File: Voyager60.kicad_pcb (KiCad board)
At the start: 2 copper layers, 285 x 95.1 mm, 265 parts, among them Q1 2N7002, SW1 5.2x5.2mm, U1 ATmega32U4-MU, U2 PRTR5V0U2X, Y1 16Mhz

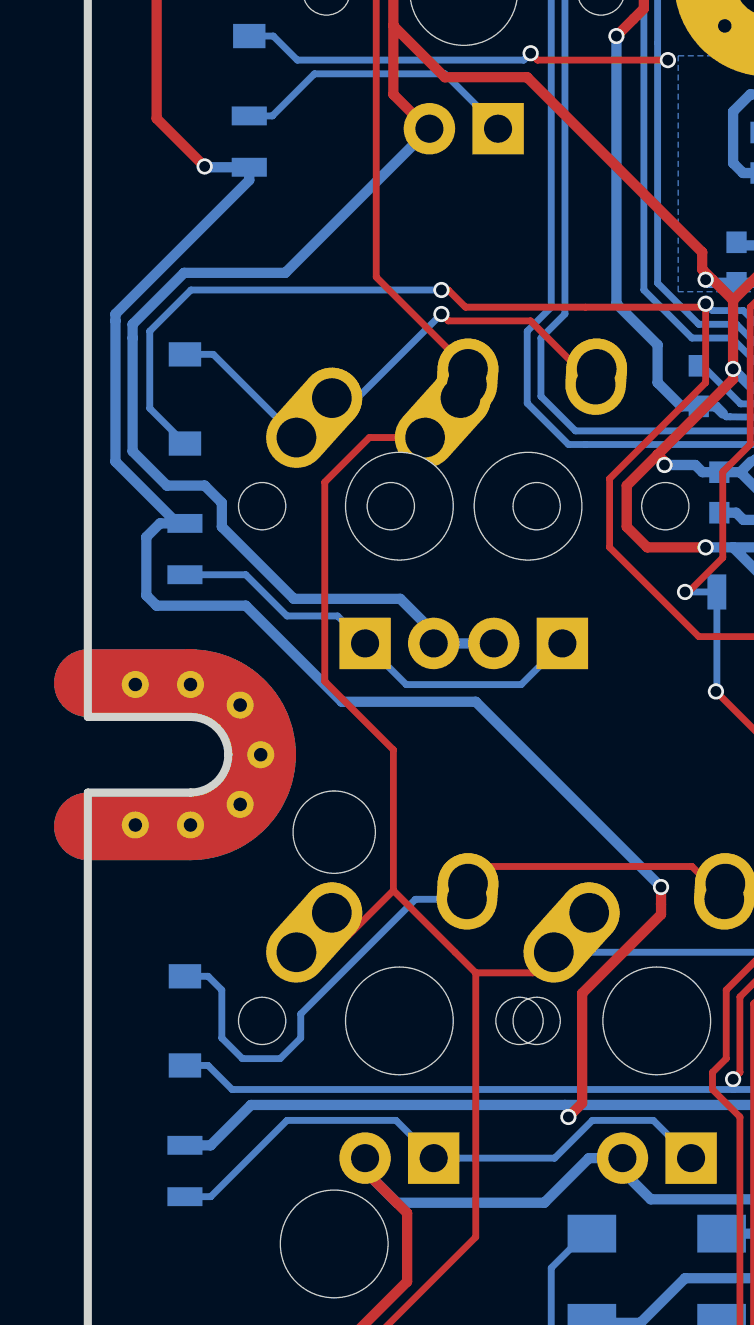
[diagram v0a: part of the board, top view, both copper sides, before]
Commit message: Alps Stepped Caps Lock
Added alps stepped caps lock support at the cost of removing caps lock LED support.
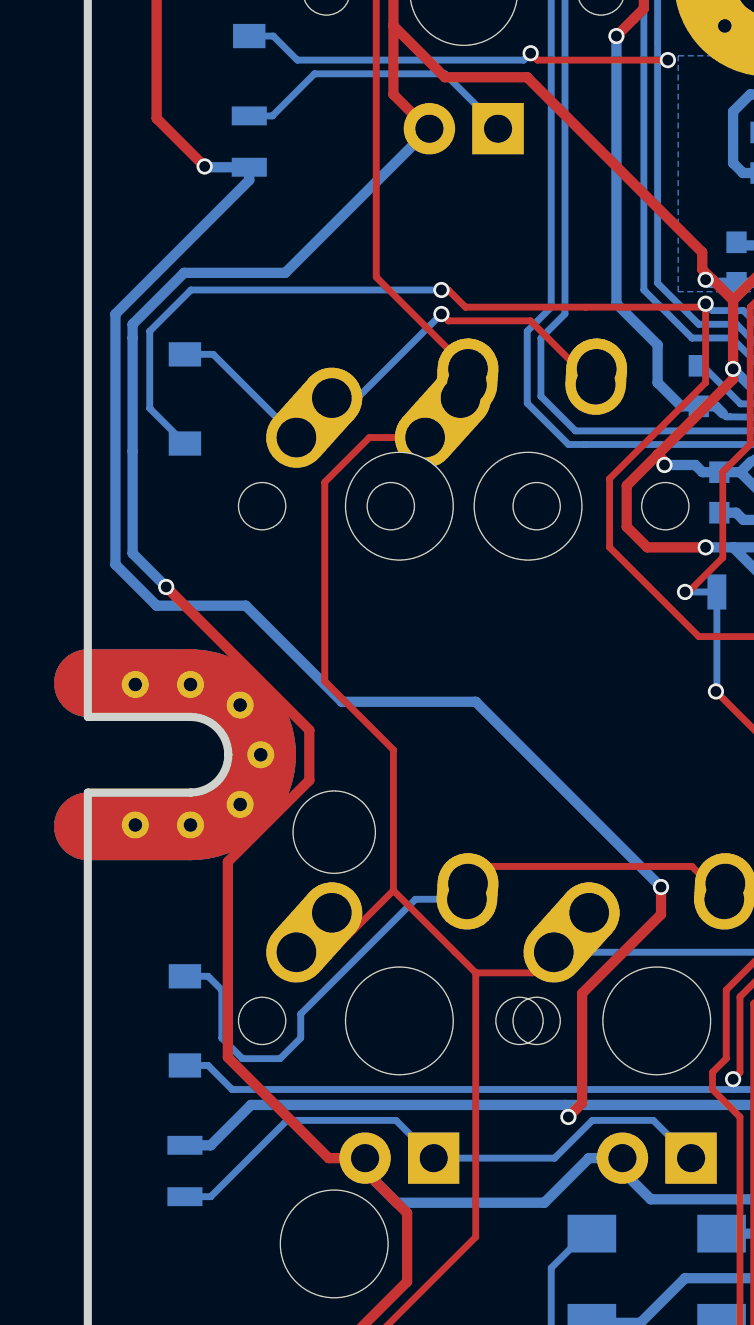
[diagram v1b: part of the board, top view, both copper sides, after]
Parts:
- removed R31: 1k, Resistors_SMD:R_0805
- K_CAPS1: value MX-1.75U -> 1.75U; footprint MX_Alps_Hybrid:MX-1.75U -> MX_Alps_Hybrid:MX-1.75U-NoLED
- K_CAPS2: footprint MX_Alps_Hybrid:MX-1.25U-FLIPPED -> MX_Alps_Hybrid:MX-1.25U-NoLED
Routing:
- net Net-(K_CAPS1-Pad4): track 16.3 -> 0.00 mm
- net +5V: track 1795.4 -> 1811.3 mm, vias 13 -> 14
- net LEDGND: track 1409.4 -> 1407.5 mm
